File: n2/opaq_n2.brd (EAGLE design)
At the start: 30.3 x 50.4 mm, 40 parts, among them IC2 TS5A3157, IC3 ATSHA204_SOIC8, IC4 ACS712, IC5 ADS1100, IC6 ATMega-328, IC7 AT25F512BWIDE_5.3MM, IC8 LM2594HV, K1 62101021021, X1 16 MHz

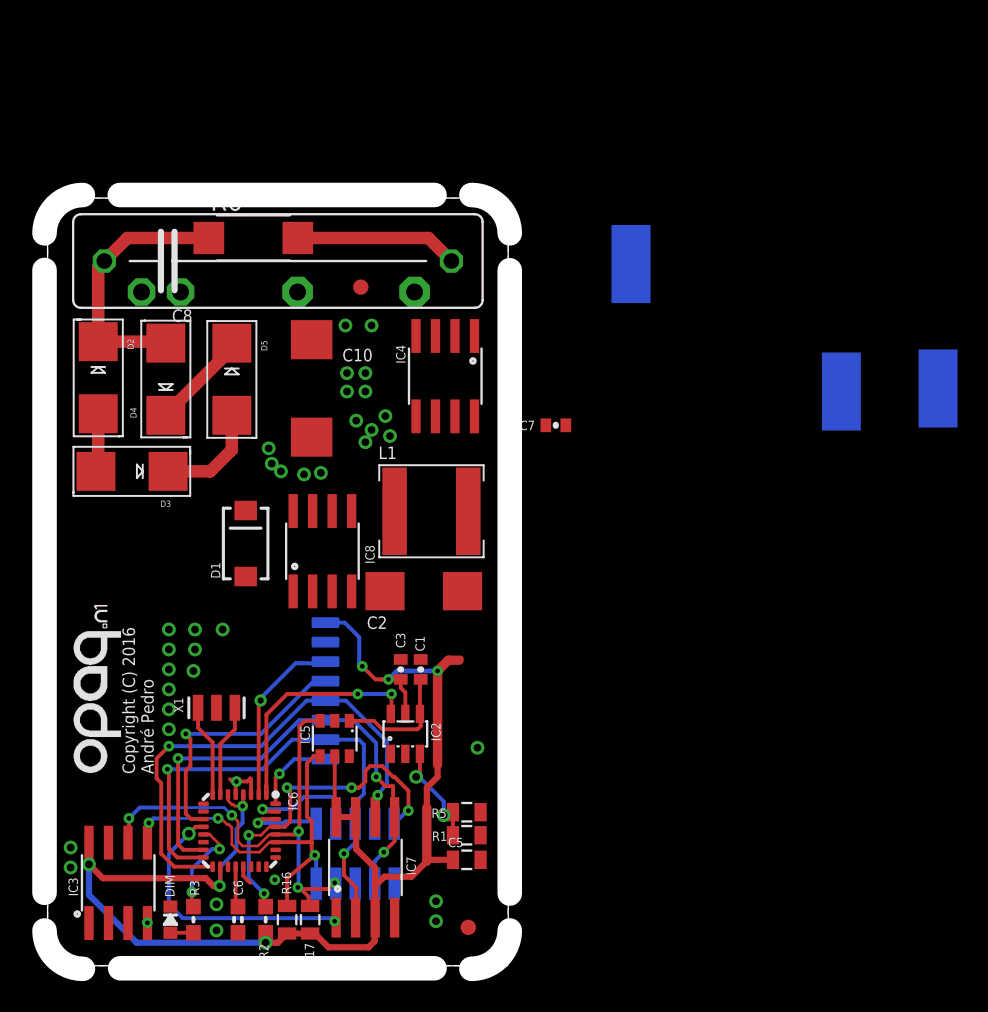
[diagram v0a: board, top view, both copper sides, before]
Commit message: Updated opaq n2 hardware. Isolated power supply has been added.
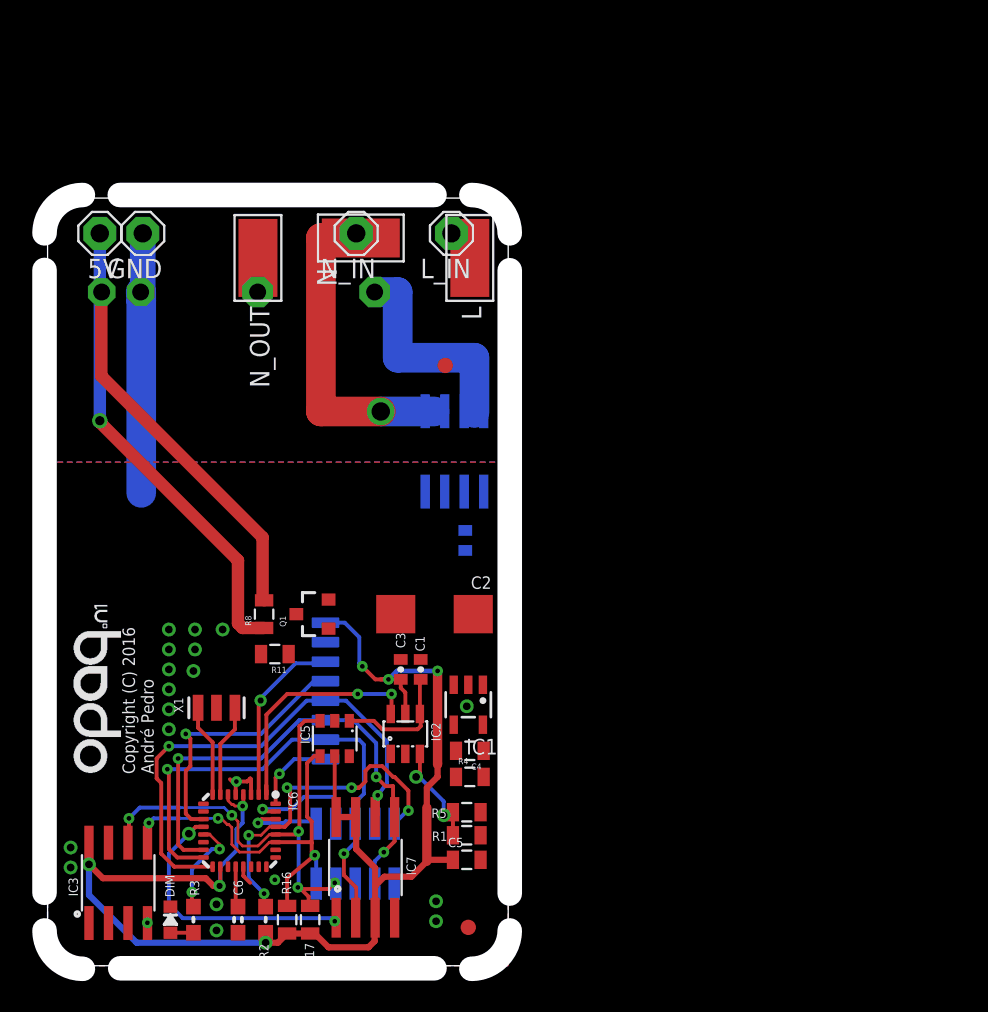
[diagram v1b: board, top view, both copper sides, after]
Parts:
- removed C10: (no value), rcl:D/7343-31R
- removed C8: (no value), resistor:C225-062X268
- removed D1: SS36, SparkFun:SMA-DIODE
- removed D2, D3, D4, D5: (no value), adafruit:SMADIODE
- removed IC8: LM2594HV, apedro_lib:SO08
- removed L1: (no value), apedro_lib:2525
- removed R6: (no value), resistor:R2512W
- removed VPLUS_IN, VPLUS_OUT: WIREPADSMD5-2,5, wirepad:5-2,5
- added 5V, L_IN, N_IN: MCS08, solpad:MCS08
- added C4: 0.1uF, SparkFun-Passives:0805
- added IC1: RT9013-XXXB, v-reg_extra:SOT23-5
- added L, N, N_OUT: WIREPADSMD5-2,5, wirepad:5-2,5
- added Q1: MMBT2222A, SparkFun-DiscreteSemi:SOT23-3
- added R11, R4, R8: (no value), resistor:0805
- GND: value WIREPADSMD5-2,5 -> MCS08; device wirepad:5-2,5 -> solpad:MCS08
- moved GND 46.7 mm to (6.20, 47.7), flipped to the top, turned to 180 degrees
- moved C7 9.54 mm to (27.2, 27.7), flipped to the bottom, turned to 270 degrees
- moved JP2 7.50 mm to (25.9, 39.1)
- moved IC4 4.94 mm to (26.5, 33.5), flipped to the bottom
- moved U$1 2.60 mm to (12.5, 45.4)
- moved C2 1.66 mm to (25.2, 22.9), turned to 0 degrees
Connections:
- removed net GND_IN: GND.1, IC4.3, IC4.4
- removed net LC: C8.1, D2.C, D4.A, R6.1
- removed net N$17: D1.C, IC8.8, L1.P$2
- removed net V+: D4.C, D5.C
- removed net V-: D2.A, D3.A
- new net N$10: IC1.3, R4.2
- new net N_IN: IC4.3, IC4.4, U$1.NO1
- new net N_OUT: N_OUT.1, U$1.NO2
- new net RELAY_C: Q1.3, R8.2, U$1.COIL2
- new net RELAY_SET: Q1.1, R11.2
- net 3.3V: now also C4.1, IC1.5, R11.1; no longer C2.+, IC8.4, L1.P$1
- net GND: now also C4.2, GND.MP, IC1.2, Q1.2, R4.1, U$1.COIL1; no longer C10.-, D1.A, IC4.1, IC4.2, IC8.5, IC8.6
- net L: now also L.1, L_IN.MP; no longer C8.2, R6.2
- net N: now also IC4.1, IC4.2, N.1, N_IN.MP; no longer D3.C, D5.A
- net VCC: now also 5V.MP, C2.+, IC1.1, R8.1
- net VPLUS_IN: no longer C10.+, IC8.7, VPLUS_IN.1, VPLUS_OUT.1
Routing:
- net VCC: track 0.00 -> 31.0 mm, vias 0 -> 1
- net RELAY_C: track 0.00 -> 24.5 mm
- net GND: track 4.45 -> 22.0 mm, vias 36 -> 20
- net LC: track 17.3 -> 0.00 mm
- net N_IN: track 0.00 -> 14.4 mm
- net N: track 6.98 -> 21.3 mm, vias 0 -> 1
- net L: track 10.6 -> 0.00 mm
- net V+: track 6.48 -> 0.00 mm
- net V-: track 3.81 -> 0.00 mm
- net 3.3V: track 91.1 -> 89.2 mm
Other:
- board text added: "Board Version 1.0 17/11/2016"
- board text removed: "Board Version 2.1 28/04/2016"

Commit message: Candidate version of opaq n2 for pcb production.
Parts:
- removed R8: (no value), resistor:0805
- added 7K471: (no value), ptc-ntc:B57164
- added CC: MCS08, solpad:MCS08
- added D1: tvs 5v, SparkFun:SOD-323
- added D2: 1N4148, SparkFun:SOD-323
- added D3: (no value), SparkFun:SMB-DIODE
- added R6, R7: (no value), resistor:0805
- added TRF250-300: (no value), fuse:TE5
- moved N_OUT 10.9 mm to (10.1, 56.4), flipped to the bottom
- moved N 10.7 mm to (14.6, 56.4), flipped to the bottom, turned to 0 degrees
- moved L 10.4 mm to (27.4, 56.5), turned to 0 degrees
- moved JP2 9.47 mm to (21.0, 31.0)
- moved R4 7.57 mm to (25.5, 19.6), turned to 270 degrees
- moved X1 2.38 mm to (11.6, 14.5), turned to 90 degrees
- moved 5V 2.19 mm to (5.40, 48.6)
- moved L_IN 2.19 mm to (28.3, 48.6)
- moved N_IN 2.19 mm to (22.1, 48.6)
- moved GND 2.19 mm to (8.20, 48.6)
- moved U$1 1.90 mm to (12.4, 43.5)
- moved C7 0.95 mm to (28.1, 27.4)
- moved C4 0.60 mm to (27.5, 13.4)
- moved C2 0.30 mm to (25.2, 22.6)
- turned R11 to 0 degrees
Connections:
- removed net DIM1: IC6.9
- removed net L: L.1, L_IN.MP
- removed net RELAY_C: Q1.3, R8.2, U$1.COIL2
- new net CC: CC.MP, IC4.3, IC4.4
- new net CURRENT_VOUT5V: IC4.7, R7.1
- new net LL: L.1, TRF250-300.1
- new net L_SAFE: 7K471.1, L_IN.MP
- new net N$3: 7K471.2, TRF250-300.2
- new net RELAY_GND: D2.2, Q1.3, U$1.COIL1
- net 3.3V: now also K1.8; no longer IC4.8
- net CURRENT_VOUT: now also R6.2, R7.2; no longer IC4.7
- net GND: now also D1.2, D3.A, R6.1; no longer U$1.COIL1
- net N: no longer IC4.1, IC4.2
- net N_IN: now also IC4.1, IC4.2; no longer IC4.3, IC4.4
- net RELAY_SET: now also IC6.9
- net VCC: now also D1.1, D2.1, D3.C, IC4.8, U$1.COIL2; no longer K1.8, R8.1
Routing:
- net VCC: track 31.0 -> 64.6 mm, vias 1 -> 4
- net RELAY_GND: track 0.00 -> 25.8 mm
- net RELAY_C: track 24.5 -> 0.00 mm
- net RELAY_SET: track 0.00 -> 19.4 mm, vias 0 -> 2
- net CURRENT_VOUT: track 0.00 -> 19.2 mm, vias 0 -> 1
- net N_OUT: track 0.00 -> 15.9 mm
- net 3.3V: track 89.2 -> 101.4 mm, vias 7 -> 11
- net GND: track 22.0 -> 32.1 mm, vias 20 -> 27
- net N: track 21.3 -> 13.4 mm, vias 1 -> 0
- net CC: track 0.00 -> 7.76 mm
- net L_SAFE: track 0.00 -> 6.16 mm
- net N_IN: track 14.4 -> 9.50 mm
- net N$3: track 0.00 -> 4.60 mm
- net LL: track 0.00 -> 3.89 mm
- net N$1: track 6.04 -> 2.29 mm
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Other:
- board size 30.3 x 50.4 mm -> 30.3 x 60.3 mm

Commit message: Opaq n2 hardware version r1.
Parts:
- moved JP2 18.1 mm to (3.00, 29.0)
- renumbered CC to RLYIN, N_OUT to RLYOUT
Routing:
- net CC: track 7.76 -> 6.58 mm
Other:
- board size 30.3 x 60.3 mm -> 30.4 x 60.3 mm
